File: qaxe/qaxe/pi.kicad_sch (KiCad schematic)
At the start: 45 parts, among them J4 Conn_01x02, J5 Conn_01x02, J5 SWD, J6 USB_C_Receptacle_USB2.0, M2 Fan_4pin, SW1 boot, U13 TMP1075, U35 STM32L151CCT6, U37 TXU0101, U39 TXU0101, X1 8MHz

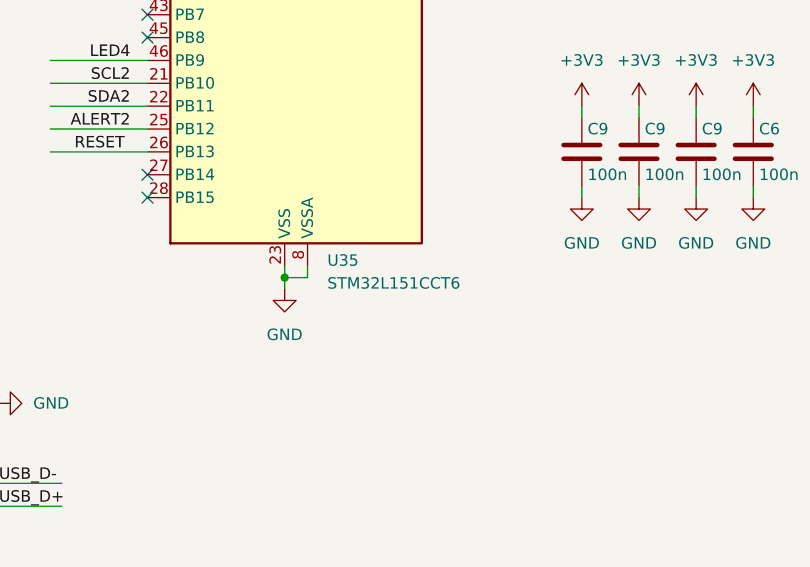
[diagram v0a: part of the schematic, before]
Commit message: updated stm32 to L072 on normal qaxe
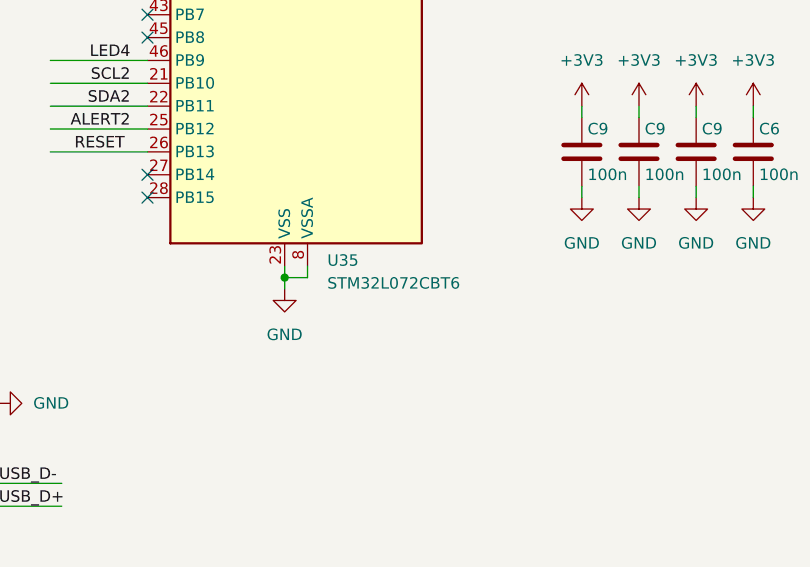
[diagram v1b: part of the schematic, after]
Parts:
- U35: value STM32L151CCT6 -> STM32L072CBT6; Manufacturer STM32L151CCT6 -> STM32L072CBT6; OrderNr 497-19371-1-ND -> 497-17503-ND
